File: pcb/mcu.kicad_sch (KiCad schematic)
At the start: 1 part, among them U3 STM32F100C4Tx

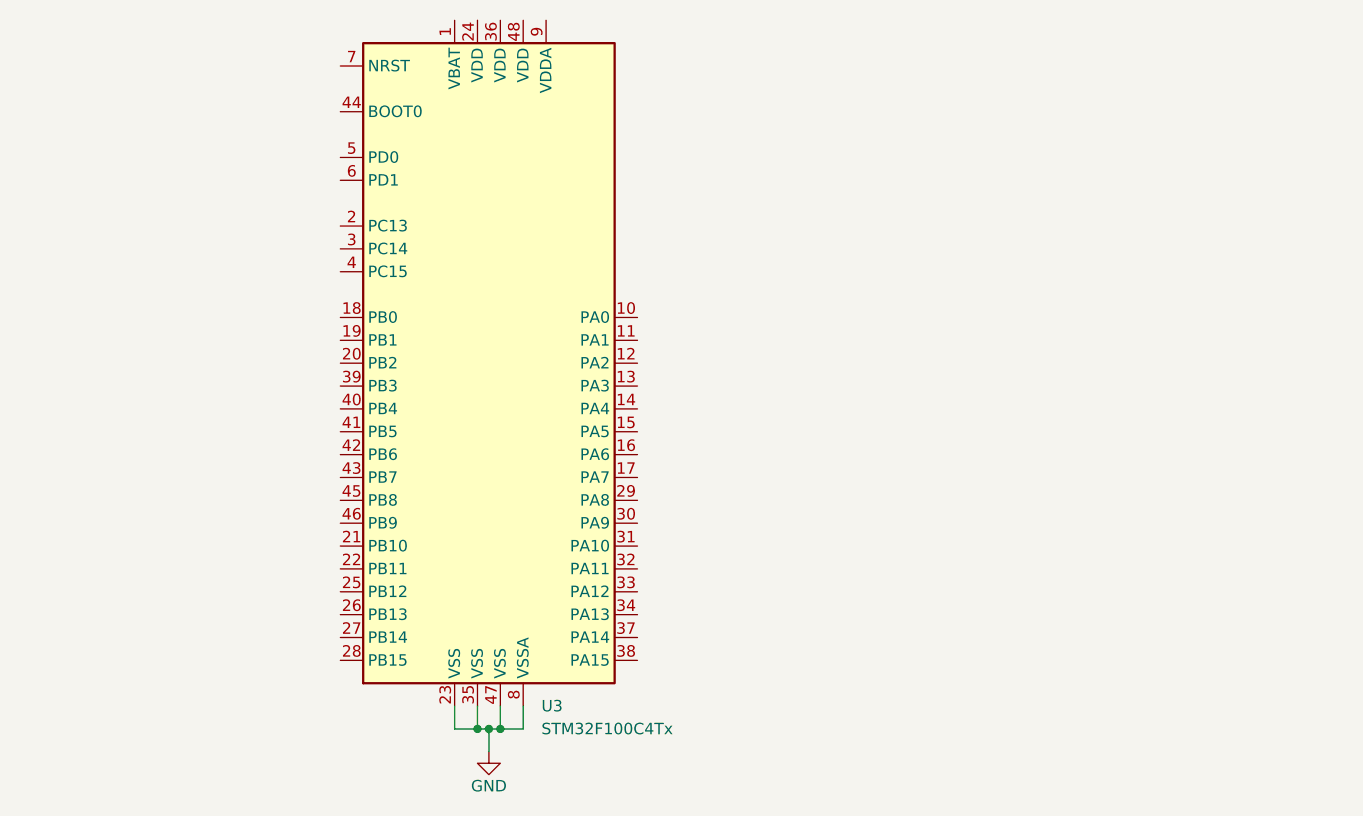
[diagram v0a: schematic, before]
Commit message: Started STM32CubeIDE project
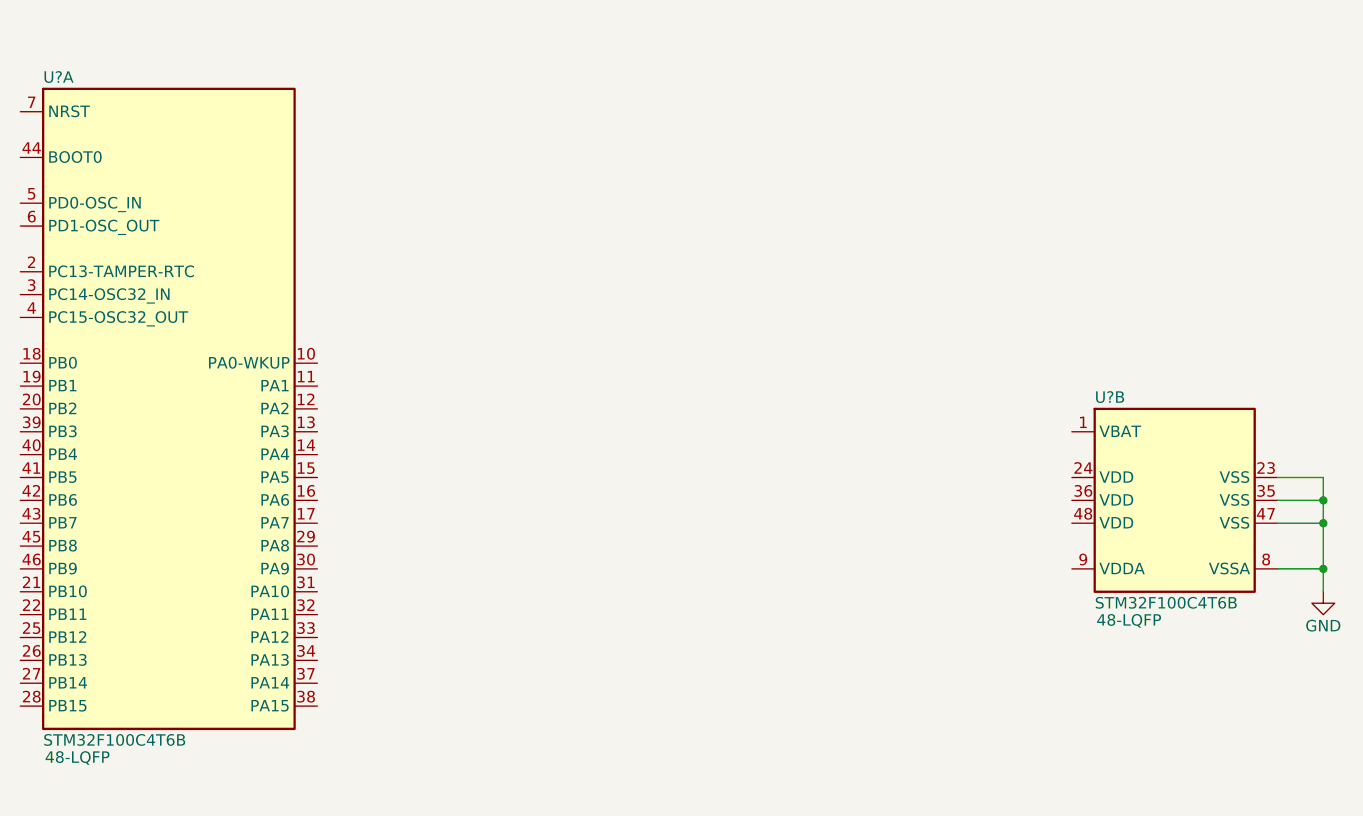
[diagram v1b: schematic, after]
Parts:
- removed U3: STM32F100C4Tx, Package_QFP:LQFP-48_7x7mm_P0.5mm, symbol MCU_ST_STM32F1:STM32F100C4Tx
- added U? (x2): IC_MCU_STM32F100C4T6B_48LQFP, Package_QFP:LQFP-48_7x7mm_P0.5mm, symbol arjun_symbols:IC_MCU_STM32F100C4T6B_48LQFP
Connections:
- net GND: now also U?.23 (VSS), U?.35 (VSS), U?.47 (VSS), U?.8 (VSSA)
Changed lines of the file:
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@@
 (kicad_sch (version 20211123) (generator eeschema)
   (paper "A4")
-  (junction (at 143.51 134.62) (diameter 0) (color 0 0 0 0)
+  (junction (at 236.22 116.84) (diameter 0) (color 0 0 0 0)
   )
-  (junction (at 144.78 134.62) (diameter 0) (color 0 0 0 0)
+  (junction (at 236.22 111.76) (diameter 0) (color 0 0 0 0)
   )
-  (junction (at 142.24 134.62) (diameter 0) (color 0 0 0 0)
+  (junction (at 236.22 109.22) (diameter 0) (color 0 0 0 0)
   )
-  (wire (pts (xy 142.24 132.08) (xy 142.24 134.62))
+  (wire (pts (xy 231.14 106.68) (xy 236.22 106.68))
     (stroke (width 0) (type default) (color 0 0 0 0))
   )
-  (wire (pts (xy 147.32 132.08) (xy 147.32 134.62))
+  (wire (pts (xy 236.22 116.84) (xy 236.22 119.38))
     (stroke (width 0) (type default) (color 0 0 0 0))
   )
-  (wire (pts (xy 144.78 134.62) (xy 143.51 134.62))
+  (wire (pts (xy 236.22 109.22) (xy 236.22 111.76))
     (stroke (width 0) (type default) (color 0 0 0 0))
   )
-  (wire (pts (xy 147.32 134.62) (xy 144.78 134.62))
+  (wire (pts (xy 236.22 106.68) (xy 236.22 109.22))
     (stroke (width 0) (type default) (color 0 0 0 0))
   )
-  (wire (pts (xy 139.7 132.08) (xy 139.7 134.62))
+  (wire (pts (xy 236.22 111.76) (xy 236.22 116.84))
     (stroke (width 0) (type default) (color 0 0 0 0))
   )
-  (wire (pts (xy 142.24 134.62) (xy 139.7 134.62))
+  (wire (pts (xy 231.14 109.22) (xy 236.22 109.22))
     (stroke (width 0) (type default) (color 0 0 0 0))
   )
-  (wire (pts (xy 143.51 134.62) (xy 143.51 137.16))
+  (wire (pts (xy 231.14 111.76) (xy 236.22 111.76))
     (stroke (width 0) (type default) (color 0 0 0 0))
   )
-  (wire (pts (xy 143.51 134.62) (xy 142.24 134.62))
+  (wire (pts (xy 231.14 116.84) (xy 236.22 116.84))
     (stroke (width 0) (type default) (color 0 0 0 0))
   )
-  (wire (pts (xy 144.78 132.08) (xy 144.78 134.62))
-    (stroke (width 0) (type default) (color 0 0 0 0))
-  )
-  (symbol (lib_id "MCU_ST_STM32F1:STM32F100C4Tx") (at 144.78 93.98 0) (unit 1)
-    (in_bom yes) (on_board yes) (fields_autoplaced)
-    (property "Reference" "U3" (id 0) (at 149.3394 132.08 0)
+  (symbol (lib_id "arjun_symbols:IC_MCU_STM32F100C4T6B_48LQFP") (at 208.28 101.6 0) (unit 2)
+    (in_bom yes) (on_board yes)
+    (property "Reference" "U?" (id 0) (at 210.82 97.79 0)
       (effects (font (size 1.27 1.27)) (justify left))
     )
-    (property "Value" "STM32F100C4Tx" (id 1) (at 149.3394 134.62 0)
+    (property "Value" "IC_MCU_STM32F100C4T6B_48LQFP" (id 1) (at 265.43 101.6 0)
+      (effects (font (size 1.27 1.27)) (justify left) hide)
+    )
+    (property "Footprint" "Package_QFP:LQFP-48_7x7mm_P0.5mm" (id 2) (at 303.53 104.14 0)
+      (effects (font (size 1.27 1.27)) (justify right) hide)
+    )
+    (property "Datasheet" "http://www.st.com/st-web-ui/static/active/en/resource/technical/document/datasheet/CD00251732.pdf" (id 3) (at 265.43 111.76 0)
+      (effects (font (size 1.27 1.27)) (justify left) hide)
+    )
+    (property "Manufacturer" "STMicroelectronics" (id 4) (at 265.43 109.22 0)
+      (effects (font (size 1.27 1.27)) (justify left) hide)
+    )
+    (property "ManufacturerPN" "STM32F100C4T6B" (id 5) (at 210.82 120.65 0)
       (effects (font (size 1.27 1.27)) (justify left))
     )
-    (property "Footprint" "Package_QFP:LQFP-48_7x7mm_P0.5mm" (id 2) (at 129.54 129.54 0)
-      (effects (font (size 1.27 1.27)) (justify right) hide)
+    (property "Vendor" "Digi-Key" (id 6) (at 265.43 114.3 0)
+      (effects (font (size 1.27 1.27)) (justify left) hide)
     )
-    (property "Datasheet" "http://www.st.com/st-web-ui/static/active/en/resource/technical/document/datasheet/CD00251732.pdf" (id 3) (at 144.78 93.98 0)
-      (effects (font (size 1.27 1.27)) hide)
+    (property "VendorPN" "497-10501-ND" (id 7) (at 265.43 116.84 0)
+      (effects (font (size 1.27 1.27)) (justify left) hide)
     )
-    (pin "1")
+    (property "Package" " 48-LQFP" (id 8) (at 214.63 122.555 0))
     (pin "10")
     (pin "11")
@@
     (pin "21")
     (pin "22")
-    (pin "23")
-    (pin "24")
     (pin "25")
     (pin "26")
@@
     (pin "33")
     (pin "34")
-    (pin "35")
-    (pin "36")
     (pin "37")
     (pin "38")
@@
     (pin "45")
     (pin "46")
-    (pin "47")
-    (pin "48")
     (pin "5")
     (pin "6")
     (pin "7")
+    (pin "1")
+    (pin "23")
+    (pin "24")
+    (pin "35")
+    (pin "36")
+    (pin "47")
+    (pin "48")
     (pin "8")
     (pin "9")
   )
-  (symbol (lib_id "power:GND") (at 143.51 137.16 0) (unit 1)
+  (symbol (lib_id "power:GND") (at 236.22 119.38 0) (unit 1)
     (in_bom yes) (on_board yes)
-    (property "Reference" "#PWR05" (id 0) (at 143.51 143.51 0)
+    (property "Reference" "#PWR05" (id 0) (at 236.22 125.73 0)
       (effects (font (size 1.27 1.27)) hide)
     )
-    (property "Value" "GND" (id 1) (at 143.51 140.97 0))
-    (property "Footprint" "" (id 2) (at 143.51 137.16 0)
+    (property "Value" "GND" (id 1) (at 236.22 123.19 0))
+    (property "Footprint" "" (id 2) (at 236.22 119.38 0)
       (effects (font (size 1.27 1.27)) hide)
     )
-    (property "Datasheet" "" (id 3) (at 143.51 137.16 0)
+    (property "Datasheet" "" (id 3) (at 236.22 119.38 0)
       (effects (font (size 1.27 1.27)) hide)
     )
     (pin "1")
   )
+  (symbol (lib_id "arjun_symbols:IC_MCU_STM32F100C4T6B_48LQFP") (at 91.44 66.04 0) (unit 1)
+    (in_bom yes) (on_board yes)
+    (property "Reference" "U?" (id 0) (at 93.98 62.23 0)
+      (effects (font (size 1.27 1.27)) (justify left))
+    )
+    (property "Value" "IC_MCU_STM32F100C4T6B_48LQFP" (id 1) (at 148.59 66.04 0)
+      (effects (font (size 1.27 1.27)) (justify left) hide)
+    )
+    (property "Footprint" "Package_QFP:LQFP-48_7x7mm_P0.5mm" (id 2) (at 186.69 68.58 0)
+      (effects (font (size 1.27 1.27)) (justify right) hide)
+    )
+    (property "Datasheet" "http://www.st.com/st-web-ui/static/active/en/resource/technical/document/datasheet/CD00251732.pdf" (id 3) (at 148.59 76.2 0)
+      (effects (font (size 1.27 1.27)) (justify left) hide)
+    )
+    (property "Manufacturer" "STMicroelectronics" (id 4) (at 148.59 73.66 0)
+      (effects (font (size 1.27 1.27)) (justify left) hide)
+    )
+    (property "ManufacturerPN" "STM32F100C4T6B" (id 5) (at 93.98 135.89 0)
+      (effects (font (size 1.27 1.27)) (justify left))
+    )
+    (property "Vendor" "Digi-Key" (id 6) (at 148.59 78.74 0)
+      (effects (font (size 1.27 1.27)) (justify left) hide)
+    )
+    (property "VendorPN" "497-10501-ND" (id 7) (at 148.59 81.28 0)
+      (effects (font (size 1.27 1.27)) (justify left) hide)
+    )
+    (property "Package" " 48-LQFP" (id 8) (at 97.79 137.795 0))
+    (pin "10")
+    (pin "11")
+    (pin "12")
+    (pin "13")
+    (pin "14")
+    (pin "15")
+    (pin "16")
+    (pin "17")
+    (pin "18")
+    (pin "19")
+    (pin "2")
+    (pin "20")
+    (pin "21")
+    (pin "22")
+    (pin "25")
+    (pin "26")
+    (pin "27")
+    (pin "28")
+    (pin "29")
+    (pin "3")
+    (pin "30")
+    (pin "31")
+    (pin "32")
+    (pin "33")
+    (pin "34")
+    (pin "37")
+    (pin "38")
+    (pin "39")
+    (pin "4")
+    (pin "40")
+    (pin "41")
+    (pin "42")
+    (pin "43")
+    (pin "44")
+    (pin "45")
+    (pin "46")
+    (pin "5")
+    (pin "6")
+    (pin "7")
+    (pin "1")
+    (pin "23")
+    (pin "24")
+    (pin "35")
+    (pin "36")
+    (pin "47")
+    (pin "48")
+    (pin "8")
+    (pin "9")
+  )
 )

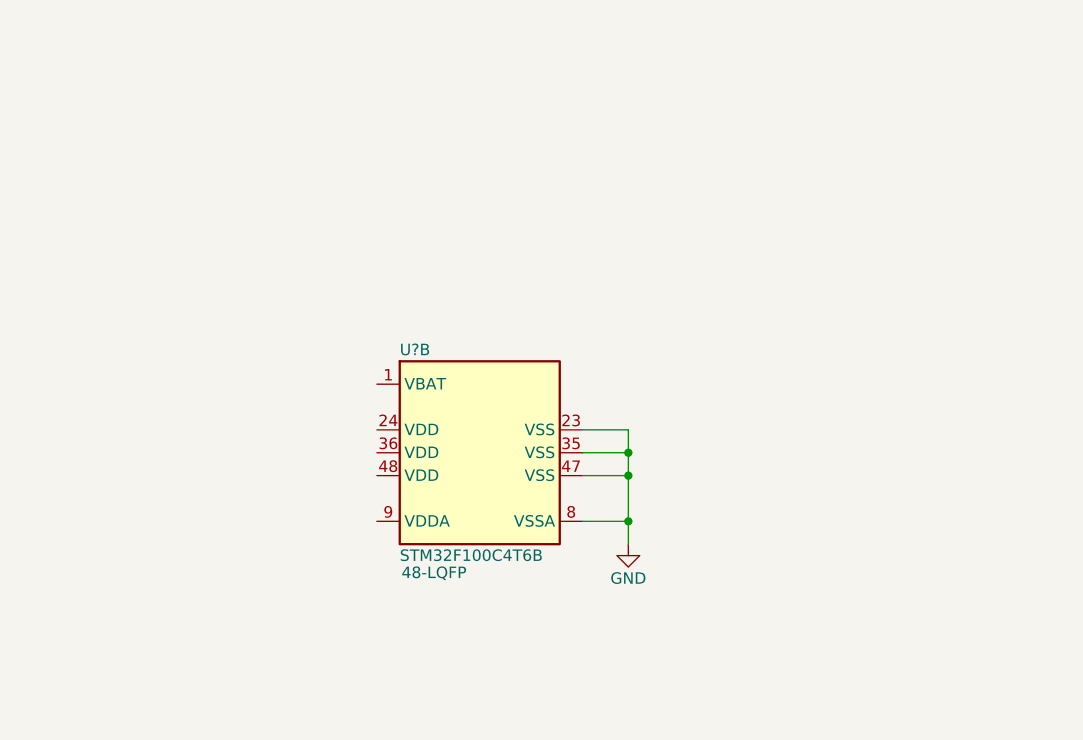
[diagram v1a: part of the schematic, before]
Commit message: Added MCU bypassing
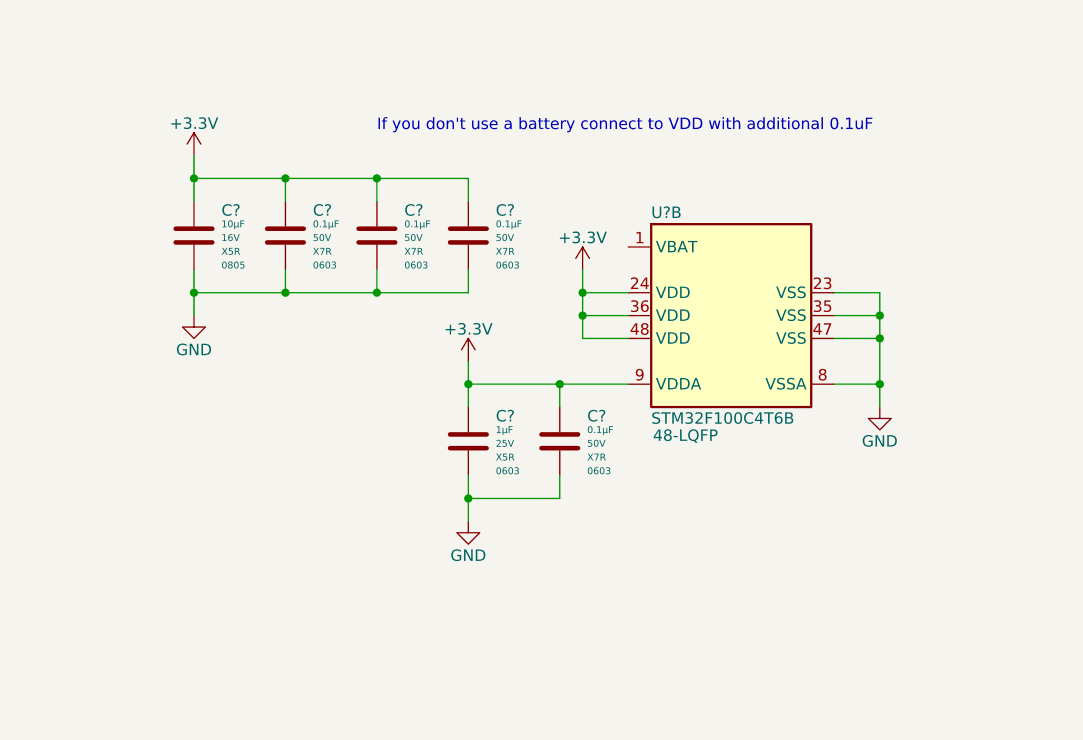
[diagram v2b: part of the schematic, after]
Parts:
- added C? (x4): CAP_CER_0u1_50V_X7R_0603, Capacitor_SMD:C_0603_1608Metric, symbol arjun_symbols:CAP_CER_0u1_50V_X7R_0603
- added C?: CAP_CER_1u_25V_X5R_0603, Capacitor_SMD:C_0603_1608Metric, symbol arjun_symbols:CAP_CER_1u_25V_X5R_0603
- added C?: CAP_CER_10u_16V_X5R_0805, Capacitor_SMD:C_0805_2012Metric, symbol arjun_symbols:CAP_CER_10u_16V_X5R_0805
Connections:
- net GND: now also C?.2, C?.2, C?.2, C?.2, C?.2, C?.2
- net +3.3V: now reaches U?.24 (VDD)
- net +3.3V: now also U?.36 (VDD), U?.48 (VDD), U?.9 (VDDA), C?.1, C?.1, C?.1, C?.1, C?.1, C?.1
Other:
- note added: "If you don't use a battery connect to VDD with additional 0.1uF"
- moved on the sheet: U?B

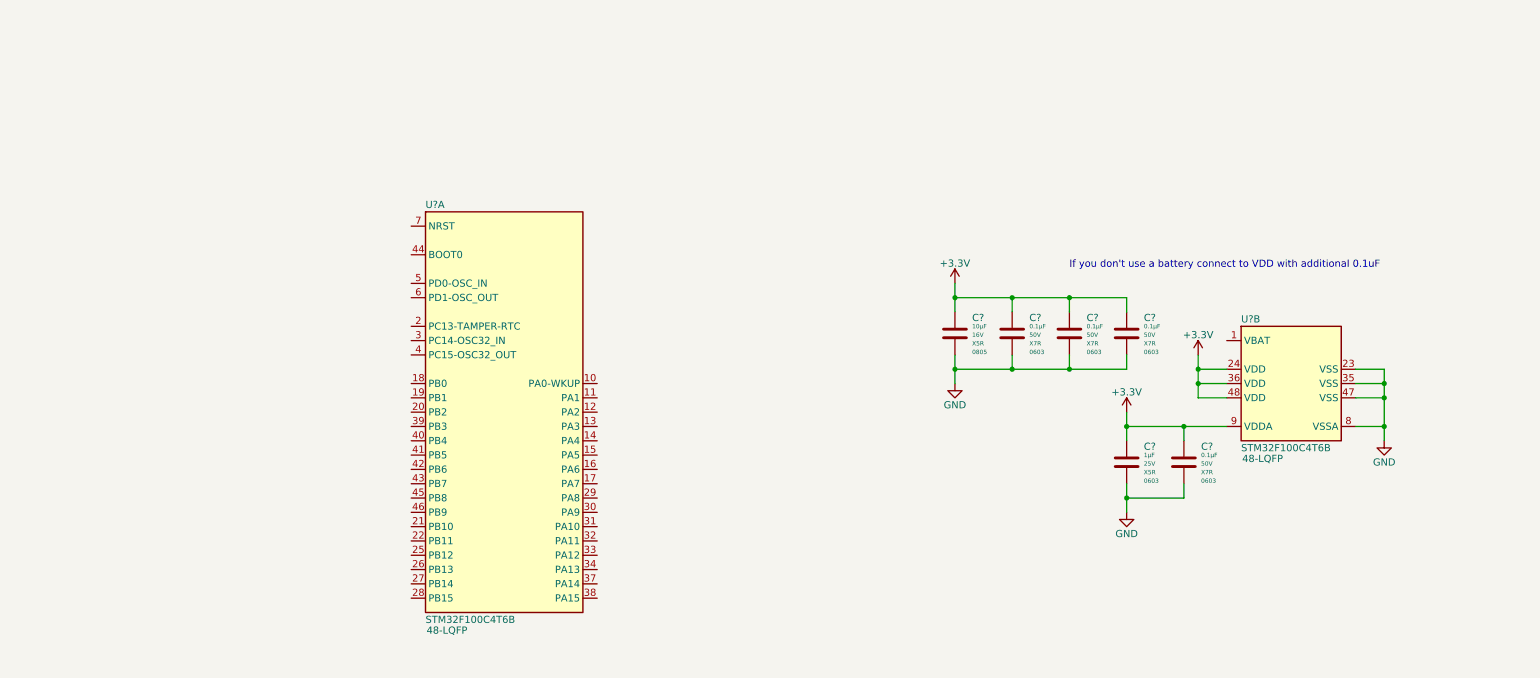
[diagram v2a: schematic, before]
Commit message: Added LSE crystal and started configuring MCU Pinout"
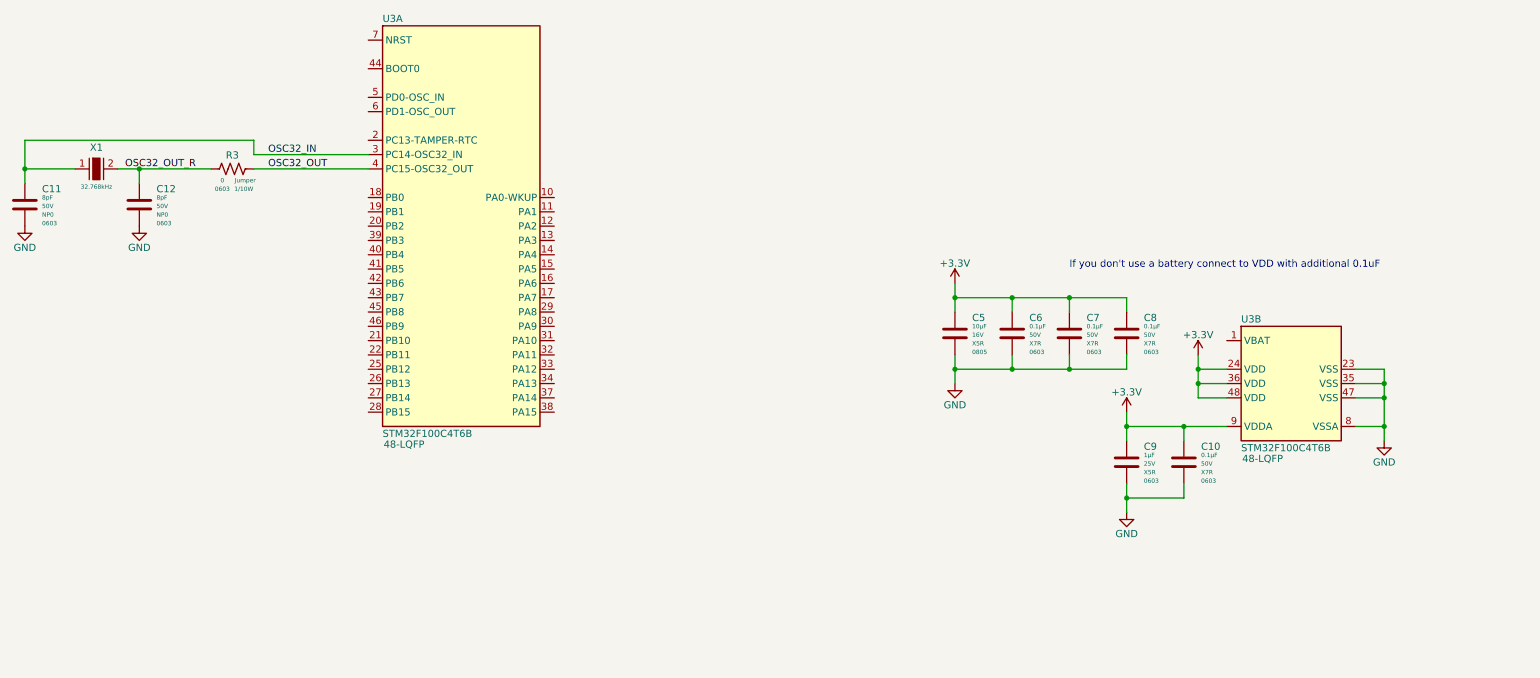
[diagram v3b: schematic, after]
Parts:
- added C11, C12: CAP_CER_8p_50V_NP0_0603, Capacitor_SMD:C_0603_1608Metric, symbol arjun_symbols:CAP_CER_8p_50V_NP0_0603
- added R3: RES_0R_1/10W_0603, Resistor_SMD:R_0603_1608Metric, symbol arjun_symbols:RES_0R_1/10W_0603
- added X1: XTAL_32K768_7pF_ECS-.327-7-34B-C-TR, arjun_footprints:SMD-2_3.2x1.5mm, symbol arjun_symbols:XTAL_32K768_7pF_ECS-.327-7-34B-C-TR
- gave numbers to parts that had none: 7
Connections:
- net GND: now also C11.2, C12.2
- net OSC32_IN: now reaches U3.3 (PC14-OSC32_IN)
- net OSC32_IN: now also C11.1, X1.1
- net OSC32_OUT: now reaches U3.4 (PC15-OSC32_OUT)
- net OSC32_OUT: now also R3.1
- new net OSC32_OUT_R: C12.1, R3.2, X1.2
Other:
- moved on the sheet: U3A
